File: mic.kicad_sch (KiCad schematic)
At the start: 3 parts

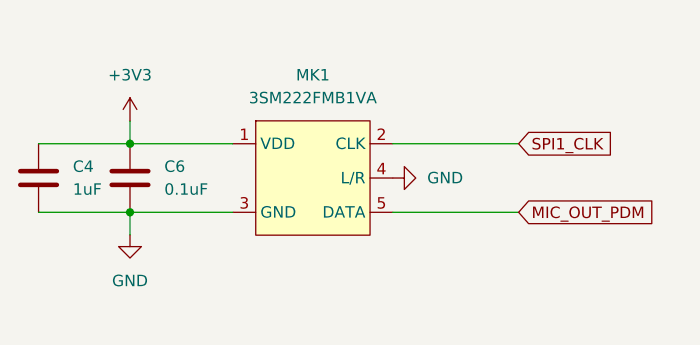
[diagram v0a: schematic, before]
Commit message: refactor hierarchical sheets to use sheet pins
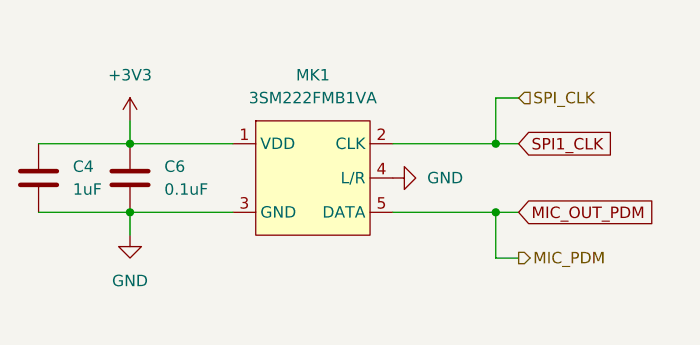
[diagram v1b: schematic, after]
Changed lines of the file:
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@@
 	(paper "A4")
 	(junction
+		(at 142.24 105.41)
+		(diameter 0)
+		(color 0 0 0 0)
+	)
+	(junction
 		(at 101.6 105.41)
 		(diameter 0)
@@
 	)
 	(junction
+		(at 142.24 97.79)
+		(diameter 0)
+		(color 0 0 0 0)
+	)
+	(junction
 		(at 101.6 97.79)
 		(diameter 0)
@@
 	(wire
 		(pts
-			(xy 130.81 105.41) (xy 144.78 105.41)
+			(xy 142.24 110.49) (xy 142.24 105.41)
+		)
+		(stroke
+			(width 0)
+			(type default)
+		)
+	)
+	(wire
+		(pts
+			(xy 142.24 105.41) (xy 144.78 105.41)
+		)
+		(stroke
+			(width 0)
+			(type default)
+		)
+	)
+	(wire
+		(pts
+			(xy 142.24 97.79) (xy 144.78 97.79)
+		)
+		(stroke
+			(width 0)
+			(type default)
+		)
+	)
+	(wire
+		(pts
+			(xy 130.81 105.41) (xy 142.24 105.41)
 		)
 		(stroke
@@
 	(wire
 		(pts
-			(xy 130.81 97.79) (xy 144.78 97.79)
+			(xy 130.81 97.79) (xy 142.24 97.79)
+		)
+		(stroke
+			(width 0)
+			(type default)
+		)
+	)
+	(wire
+		(pts
+			(xy 144.78 110.49) (xy 142.24 110.49)
 		)
 		(stroke
@@
 	(wire
 		(pts
+			(xy 144.78 92.71) (xy 142.24 92.71)
+		)
+		(stroke
+			(width 0)
+			(type default)
+		)
+	)
+	(wire
+		(pts
 			(xy 101.6 107.95) (xy 101.6 105.41)
 		)
@@
 		(pts
 			(xy 101.6 97.79) (xy 113.03 97.79)
+		)
+		(stroke
+			(width 0)
+			(type default)
+		)
+	)
+	(wire
+		(pts
+			(xy 142.24 92.71) (xy 142.24 97.79)
 		)
 		(stroke
@@
 		)
 	)
+	(hierarchical_label "MIC_PDM"
+		(shape output)
+		(at 144.78 110.49 0)
+		(effects
+			(font
+				(size 1.27 1.27)
+			)
+			(justify left)
+		)
+	)
+	(hierarchical_label "SPI_CLK"
+		(shape input)
+		(at 144.78 92.71 0)
+		(effects
+			(font
+				(size 1.27 1.27)
+			)
+			(justify left)
+		)
+	)

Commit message: WIP relayout of board
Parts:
- C4, C6: footprint Capacitor_SMD:C_0603_1608Metric -> Capacitor_SMD:C_0402_1005Metric
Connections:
- net MIC_OUT_PDM renamed MIC_PDM
- net SPI1_CLK renamed SPI_CLK
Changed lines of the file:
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@@
 	(generator_version "9.0")
 	(paper "A4")
-	(junction
-		(at 142.24 105.41)
-		(diameter 0)
-		(color 0 0 0 0)
+	(rectangle
+		(start 107.95 83.82)
+		(end 137.16 118.11)
+		(stroke
+			(width 0)
+			(type default)
+		)
+		(fill
+			(type none)
+		)
 	)
 	(junction
@@
 	)
 	(junction
-		(at 142.24 97.79)
-		(diameter 0)
-		(color 0 0 0 0)
-	)
-	(junction
 		(at 101.6 97.79)
 		(diameter 0)
@@
 	(wire
 		(pts
-			(xy 142.24 110.49) (xy 142.24 105.41)
-		)
-		(stroke
-			(width 0)
-			(type default)
-		)
-	)
-	(wire
-		(pts
-			(xy 142.24 105.41) (xy 144.78 105.41)
-		)
-		(stroke
-			(width 0)
-			(type default)
-		)
-	)
-	(wire
-		(pts
-			(xy 142.24 97.79) (xy 144.78 97.79)
-		)
-		(stroke
-			(width 0)
-			(type default)
-		)
-	)
-	(wire
-		(pts
-			(xy 130.81 105.41) (xy 142.24 105.41)
+			(xy 130.81 105.41) (xy 146.05 105.41)
 		)
 		(stroke
@@
 	(wire
 		(pts
-			(xy 130.81 97.79) (xy 142.24 97.79)
-		)
-		(stroke
-			(width 0)
-			(type default)
-		)
-	)
-	(wire
-		(pts
-			(xy 144.78 110.49) (xy 142.24 110.49)
+			(xy 130.81 97.79) (xy 146.05 97.79)
 		)
 		(stroke
@@
 	(wire
 		(pts
-			(xy 144.78 92.71) (xy 142.24 92.71)
-		)
-		(stroke
-			(width 0)
-			(type default)
-		)
-	)
-	(wire
-		(pts
 			(xy 101.6 107.95) (xy 101.6 105.41)
 		)
@@
 	(wire
 		(pts
-			(xy 142.24 92.71) (xy 142.24 97.79)
-		)
-		(stroke
-			(width 0)
-			(type default)
-		)
-	)
-	(wire
-		(pts
 			(xy 101.6 95.25) (xy 101.6 97.79)
 		)
@@
 		)
 	)
-	(global_label "MIC_OUT_PDM"
-		(shape input)
-		(at 144.78 105.41 0)
-		(fields_autoplaced yes)
+	(hierarchical_label "MIC_PDM"
+		(shape output)
+		(at 146.05 105.41 0)
 		(effects
 			(font
@@
 			(justify left)
 		)
-		(property "Intersheetrefs" "${INTERSHEET_REFS}"
-			(at 160.6466 105.41 0)
-			(effects
-				(font
-					(size 1.27 1.27)
-				)
-				(justify left)
-				(hide yes)
-			)
-		)
-	)
-	(global_label "SPI1_CLK"
-		(shape input)
-		(at 144.78 97.79 0)
-		(fields_autoplaced yes)
-		(effects
-			(font
-				(size 1.27 1.27)
-			)
-			(justify left)
-		)
-		(property "Intersheetrefs" "${INTERSHEET_REFS}"
-			(at 156.5947 97.79 0)
-			(effects
-				(font
-					(size 1.27 1.27)
-				)
-				(justify left)
-				(hide yes)
-			)
-		)
-	)
-	(hierarchical_label "MIC_PDM"
-		(shape output)
-		(at 144.78 110.49 0)
-		(effects
-			(font
-				(size 1.27 1.27)
-			)
-			(justify left)
-		)
 	)
 	(hierarchical_label "SPI_CLK"
 		(shape input)
-		(at 144.78 92.71 0)
+		(at 146.05 97.79 0)
 		(effects
 			(font
@@
 			)
 		)
-		(property "Footprint" "Capacitor_SMD:C_0603_1608Metric"
+		(property "Footprint" "Capacitor_SMD:C_0402_1005Metric"
 			(at 102.5652 105.41 0)
 			(effects
@@
 			)
 		)
-		(property "Footprint" "Capacitor_SMD:C_0603_1608Metric"
+		(property "Footprint" "Capacitor_SMD:C_0402_1005Metric"
 			(at 92.4052 105.41 0)
 			(effects

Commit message: Board V3
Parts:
- C4: Est Cost 0.0027 -> (none); Est Cost (1000) (none) -> 0.001; LCSC (none) -> https://www.lcsc.com/product-detail/C7503520.html; Manufacturer (none) -> HRE; Part No (none) -> CGA0402X5R105K100GT; Type (none) -> SMD; Vendor https://www.lcsc.com/product-detail/C6119818.html -> (none)
- C6: value 0.1uF -> 100nF; Est Cost 0.002 -> (none); Est Cost (1000) (none) -> 0.0007; LCSC (none) -> https://www.lcsc.com/product-detail/C22435938.html; Manufacturer (none) -> HRE; Part No (none) -> CGA0402X7R104K6R3GT; Type (none) -> SMD; Vendor https://www.lcsc.com/product-detail/C6119883.html -> (none)
- MK1: Digikey (none) -> https://www.digikey.com.au/en/products/detail/3s-solid-stat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; Est Cost 0.33178 -> (none); Est Cost (1000) (none) -> 0.33178; Height (none) -> 1mm; Manufacturer (none) -> 3S (Solid State System); Part No (none) -> 3SM222FMB1VA; Type (none) -> SMD; Vendor https://www.digikey.com.au/en/products/detail/3s-solid-stat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 -> (none)
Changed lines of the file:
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@@
 	(generator_version "9.0")
 	(paper "A4")
-	(rectangle
-		(start 107.95 83.82)
-		(end 137.16 118.11)
-		(stroke
-			(width 0)
-			(type default)
-		)
-		(fill
-			(type none)
-		)
-	)
 	(junction
 		(at 101.6 105.41)
@@
 			)
 		)
-		(property "Value" "0.1uF"
+		(property "Value" "100nF"
 			(at 105.41 102.8699 0)
 			(effects
@@
 			)
 		)
-		(property "Description" "Unpolarized capacitor"
-			(at 101.6 101.6 0)
-			(effects
-				(font
-					(size 1.27 1.27)
-				)
-				(hide yes)
-			)
-		)
-		(property "Vendor" "https://www.lcsc.com/product-detail/C6119883.html"
-			(at 101.6 101.6 0)
-			(effects
-				(font
-					(size 1.27 1.27)
-				)
-				(hide yes)
-			)
-		)
-		(property "Est Cost" "0.002"
+		(property "Description" "100nF ±10% 6.3V Ceramic Capacitor X7R 0402"
+			(at 101.6 101.6 0)
+			(effects
+				(font
+					(size 1.27 1.27)
+				)
+				(hide yes)
+			)
+		)
+		(property "Est Cost" ""
 			(at 101.6 101.6 0)
 			(effects
@@
 		)
 		(property "Field6" ""
+			(at 101.6 101.6 0)
+			(effects
+				(font
+					(size 1.27 1.27)
+				)
+				(hide yes)
+			)
+		)
+		(property "Alibaba" ""
+			(at 101.6 101.6 0)
+			(effects
+				(font
+					(size 1.27 1.27)
+				)
+				(hide yes)
+			)
+		)
+		(property "Est Cost (1000)" "0.0007"
+			(at 101.6 101.6 0)
+			(effects
+				(font
+					(size 1.27 1.27)
+				)
+				(hide yes)
+			)
+		)
+		(property "LCSC" "https://www.lcsc.com/product-detail/C22435938.html"
+			(at 101.6 101.6 0)
+			(effects
+				(font
+					(size 1.27 1.27)
+				)
+				(hide yes)
+			)
+		)
+		(property "Manufacturer" "HRE"
+			(at 101.6 101.6 0)
+			(effects
+				(font
+					(size 1.27 1.27)
+				)
+				(hide yes)
+			)
+		)
+		(property "Part No" "CGA0402X7R104K6R3GT"
+			(at 101.6 101.6 0)
+			(effects
+				(font
+					(size 1.27 1.27)
+				)
+				(hide yes)
+			)
+		)
+		(property "Digikey" ""
+			(at 101.6 101.6 0)
+			(effects
+				(font
+					(size 1.27 1.27)
+				)
+				(hide yes)
+			)
+		)
+		(property "Type" "SMD"
 			(at 101.6 101.6 0)
 			(effects
@@
 			)
 		)
-		(property "Description" "3SM222FMB1VA MEMS Microphone IC"
-			(at 121.92 93.98 0)
-			(effects
-				(font
-					(size 1.27 1.27)
-				)
-				(hide yes)
-			)
-		)
-		(property "Est Cost" "0.33178"
-			(at 121.92 93.98 0)
-			(effects
-				(font
-					(size 1.27 1.27)
-				)
-				(hide yes)
-			)
-		)
-		(property "Vendor" "https://www.digikey.com.au/en/products/detail/3s-solid-state-system/3SM222FMB1VA/25559041"
+		(property "Description" "100 Hz ~ 10 kHz Digital, PDM Microphone MEMS (Silicon) 1.6 V ~ 3.6 V Omnidirectional (-26dB ±1dB @ 94dB SPL) Solder Pads"
+			(at 121.92 93.98 0)
+			(effects
+				(font
+					(size 1.27 1.27)
+				)
+				(hide yes)
+			)
+		)
+		(property "Est Cost" ""
 			(at 121.92 93.98 0)
 			(effects
@@
 		)
 		(property "Field6" ""
+			(at 121.92 93.98 0)
+			(effects
+				(font
+					(size 1.27 1.27)
+				)
+				(hide yes)
+			)
+		)
+		(property "Alibaba" ""
+			(at 121.92 93.98 0)
+			(effects
+				(font
+					(size 1.27 1.27)
+				)
+				(hide yes)
+			)
+		)
+		(property "Digikey" "https://www.digikey.com.au/en/products/detail/3s-solid-state-system/3SM222FMB1VA/25559041"
+			(at 121.92 93.98 0)
+			(effects
+				(font
+					(size 1.27 1.27)
+				)
+				(hide yes)
+			)
+		)
+		(property "Est Cost (1000)" "0.33178"
+			(at 121.92 93.98 0)
+			(effects
+				(font
+					(size 1.27 1.27)
+				)
+				(hide yes)
+			)
+		)
+		(property "Manufacturer" "3S (Solid State System)"
+			(at 121.92 93.98 0)
+			(effects
+				(font
+					(size 1.27 1.27)
+				)
+				(hide yes)
+			)
+		)
+		(property "Part No" "3SM222FMB1VA"
+			(at 121.92 93.98 0)
+			(effects
+				(font
+					(size 1.27 1.27)
+				)
+				(hide yes)
+			)
+		)
+		(property "Height" "1mm"
+			(at 121.92 93.98 0)
+			(effects
+				(font
+					(size 1.27 1.27)
+				)
+				(hide yes)
+			)
+		)
+		(property "Type" "SMD"
 			(at 121.92 93.98 0)
 			(effects
@@
 			)
 		)
-		(property "Description" "Unpolarized capacitor"
-			(at 91.44 101.6 0)
-			(effects
-				(font
-					(size 1.27 1.27)
-				)
-				(hide yes)
-			)
-		)
-		(property "Vendor" "https://www.lcsc.com/product-detail/C6119818.html"
-			(at 91.44 101.6 0)
-			(effects
-				(font
-					(size 1.27 1.27)
-				)
-				(hide yes)
-			)
-		)
-		(property "Est Cost" "0.0027"
+		(property "Description" "1uF ±10% 10V Ceramic Capacitor X5R 0402"
+			(at 91.44 101.6 0)
+			(effects
+				(font
+					(size 1.27 1.27)
+				)
+				(hide yes)
+			)
+		)
+		(property "Est Cost" ""
 			(at 91.44 101.6 0)
 			(effects
@@
 			(at 91.44 101.6 0)
 			(effects
+				(font
+					(size 1.27 1.27)
+				)
+				(hide yes)
+			)
+		)
+		(property "Alibaba" ""
+			(at 91.44 101.6 0)
+			(effects
+				(font
+					(size 1.27 1.27)
+				)
+				(hide yes)
+			)
+		)
+		(property "Est Cost (1000)" "0.001"
+			(at 91.44 101.6 0)
+			(effects
+				(font
+					(size 1.27 1.27)
+				)
+				(hide yes)
+			)
+		)
+		(property "LCSC" "https://www.lcsc.com/product-detail/C7503520.html"
+			(at 91.44 101.6 0)
+			(effects
+				(font
+					(size 1.27 1.27)
+				)
+				(hide yes)
+			)
+		)
+		(property "Manufacturer" "HRE"
+			(at 91.44 101.6 0)
+			(effects
+				(font
+					(size 1.27 1.27)
+				)
+				(hide yes)
+			)
+		)
+		(property "Part No" "CGA0402X5R105K100GT"
+			(at 91.44 101.6 0)
+			(effects
+				(font
+					(size 1.27 1.27)
+				)
+				(hide yes)
+			)
+		)
+		(property "Digikey" ""
+			(at 91.44 101.6 0)
+			(effects
+				(font
+					(size 1.27 1.27)
+				)
+				(hide yes)
+			)
+		)
+		(property "Type" "SMD"
+			(at 91.44 101.6 0)
+			(effects
